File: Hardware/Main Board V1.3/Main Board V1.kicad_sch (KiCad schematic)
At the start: 96 parts, among them J1 AUX GPIO, J10 Module 2, J11 VMot, J12 Module 3, J13 Shift Regs and Motor Drvs, J14 Module 4, J15 Module 5, J16 Micro_SD_Card, J17 Pin, J18 Pin, J19 Pin, J20 Pin, J21 Pin, J22 Pin, J23 RST, J24 RST, J3 Torch module, J4 Jumper, J5 Motor, J6 Module 1, J7 Ext Mot Drv, J8 01x02, J9 THC_Display, U1 ESP32_38p, U10 Y, U11 z, U12 A, U13 B, U14 C, U2 74LVC157A, U3 ESP32_38p, U4 BL8071CLATR33, U5 74AHCT595, U6 74AHCT595, U7 74AHCT595, U8 74AHCT595, U9 X

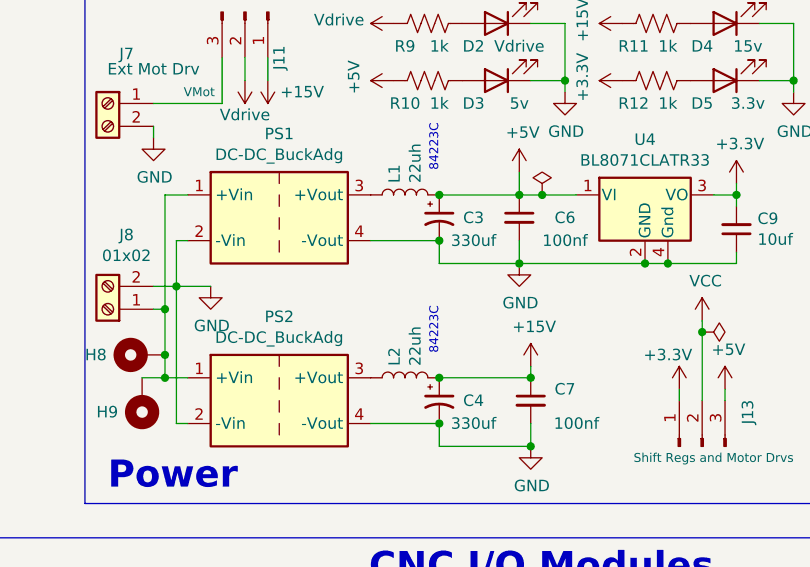
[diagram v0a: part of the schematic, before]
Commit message: add smps for 5v and 12v, add more module prototypes
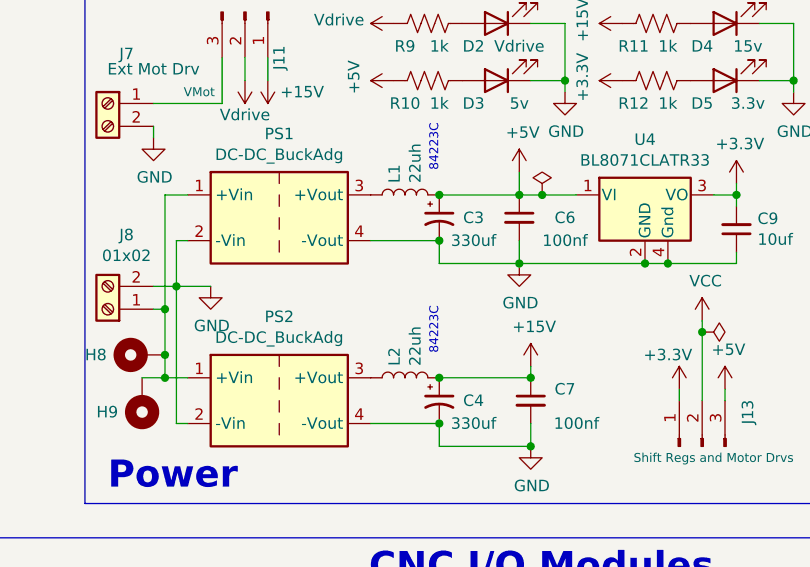
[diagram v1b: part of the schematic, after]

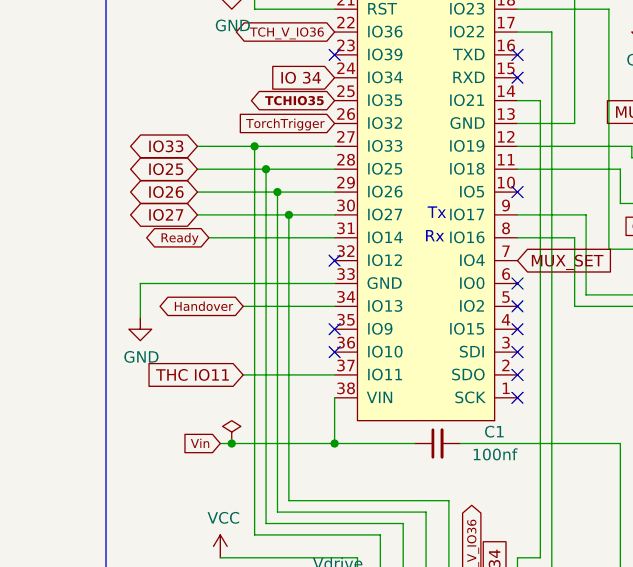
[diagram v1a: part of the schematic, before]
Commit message: Pin Mapping update
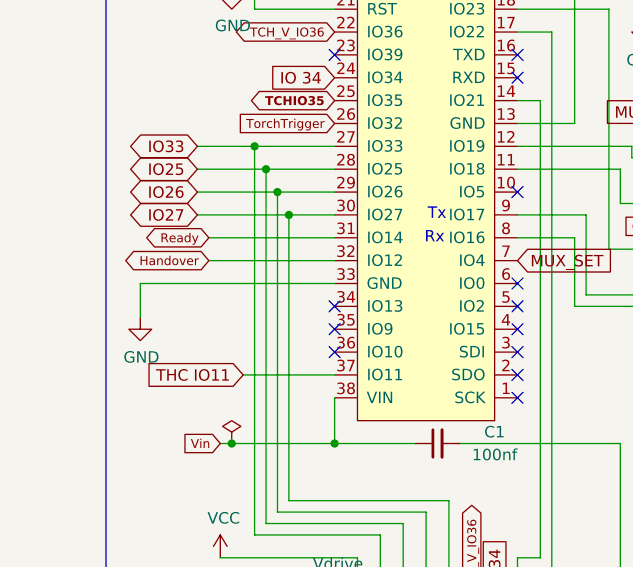
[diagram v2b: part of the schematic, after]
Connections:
- net Handover: now also U1.32 (IO12); no longer U1.34 (IO13)
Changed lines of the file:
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@@
   )
   (no_connect (at 213.36 85.09))
-  (no_connect (at 101.6 63.5))
   (no_connect (at 346.71 54.61))
   (no_connect (at 88.9 135.89))
@@
   (no_connect (at 101.6 71.12))
   (no_connect (at 142.24 64.77))
+  (no_connect (at 101.6 68.58))
   (no_connect (at 158.75 66.04))
   (no_connect (at 121.92 68.58))
@@
     (stroke (width 0) (type default))
   )
-  (wire (pts (xy 91.44 68.58) (xy 101.6 68.58))
+  (wire (pts (xy 87.63 63.5) (xy 101.6 63.5))
     (stroke (width 0) (type default))
   )
@@
     )
   )
-  (global_label "Handover" (shape bidirectional) (at 91.44 68.58 180) (fields_autoplaced)
+  (global_label "Handover" (shape bidirectional) (at 87.63 63.5 180) (fields_autoplaced)
     (effects (font (size 0.9906 0.9906)) (justify right))
-    (property "Intersheetrefs" "${INTERSHEET_REFS}" (at 3.81 5.08 0)
+    (property "Intersheetrefs" "${INTERSHEET_REFS}" (at 0 0 0)
       (effects (font (size 1.27 1.27)) hide)
     )

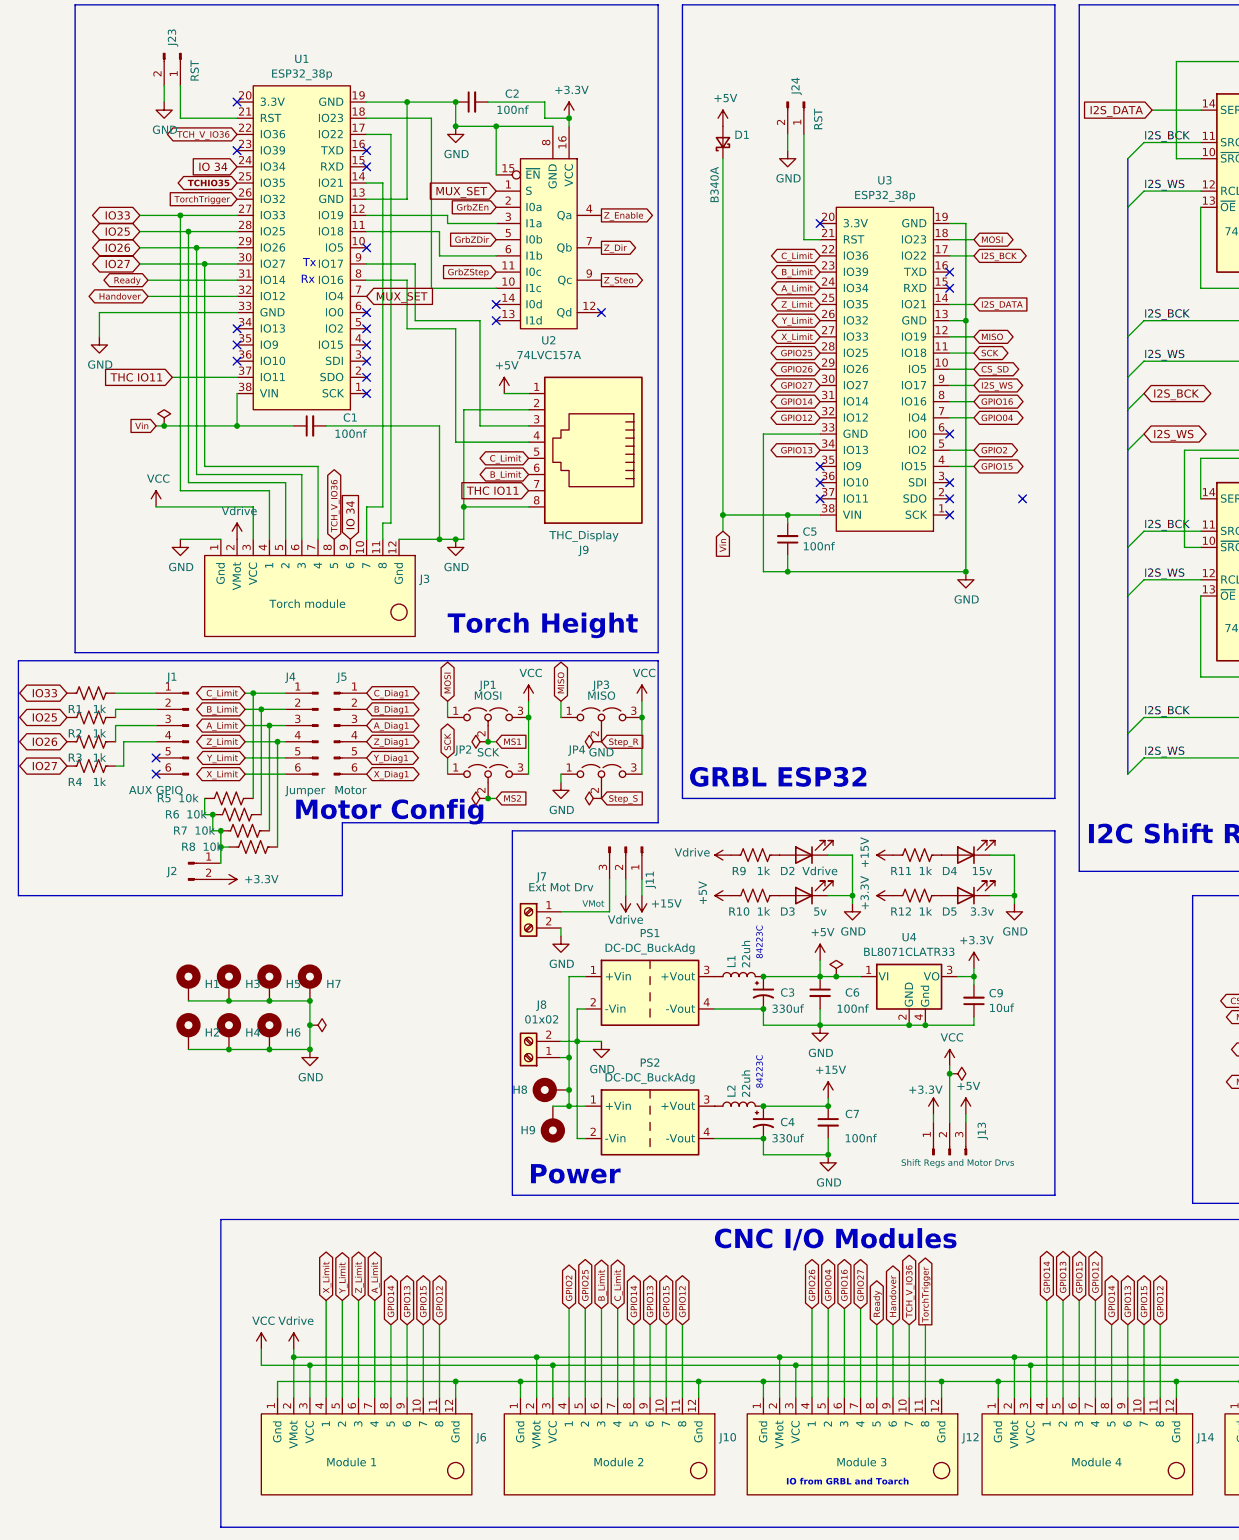
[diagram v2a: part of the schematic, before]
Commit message: Pin Naming Changes
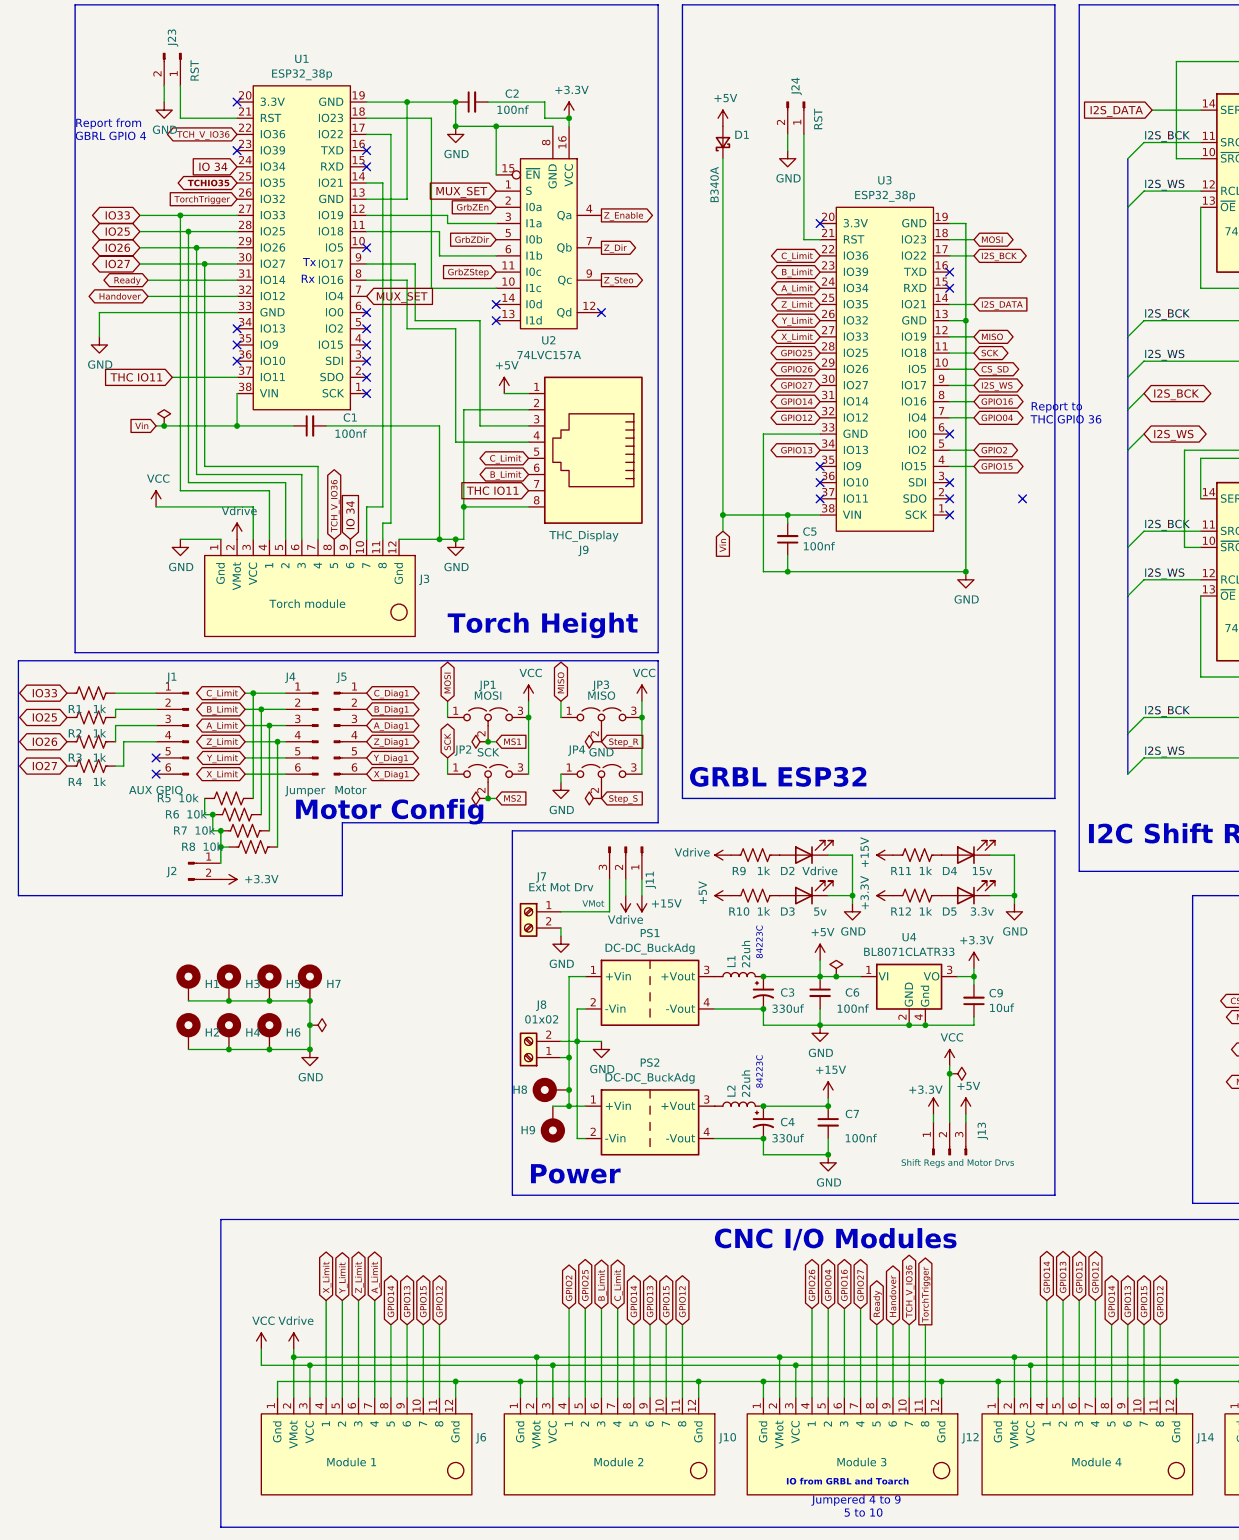
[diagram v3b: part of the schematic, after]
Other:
- note added: "Jumpered 4 to 9 5 to 10"
- note added: "Report from GBRL GPIO 4"
- note added: "Report to THC GPIO 36"
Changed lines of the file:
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@@
     (effects (font (size 2.9972 2.9972) (thickness 0.5994) bold) (justify right bottom))
+  )
+  (text "Report to \nTHC GPIO 36" (at 226.06 83.82 0)
+    (effects (font (size 1.27 1.27)) (justify left bottom))
+  )
+  (text "Jumpered 4 to 9\n         5 to 10" (at 191.77 255.27 0)
+    (effects (font (size 1.27 1.27)) (justify left bottom))
   )
   (text "84223C" (at 184.15 167.64 90)
@@
     (effects (font (size 0.9906 0.9906) (thickness 0.1981) bold) (justify right bottom))
   )
+  (text "Report from \nGBRL GPIO 4" (at 76.2 39.37 0)
+    (effects (font (size 1.27 1.27)) (justify left bottom))
+  )
   (text "Motor Drivers" (at 328.93 231.14 0)
